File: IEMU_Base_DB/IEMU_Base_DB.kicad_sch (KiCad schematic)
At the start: 0 parts

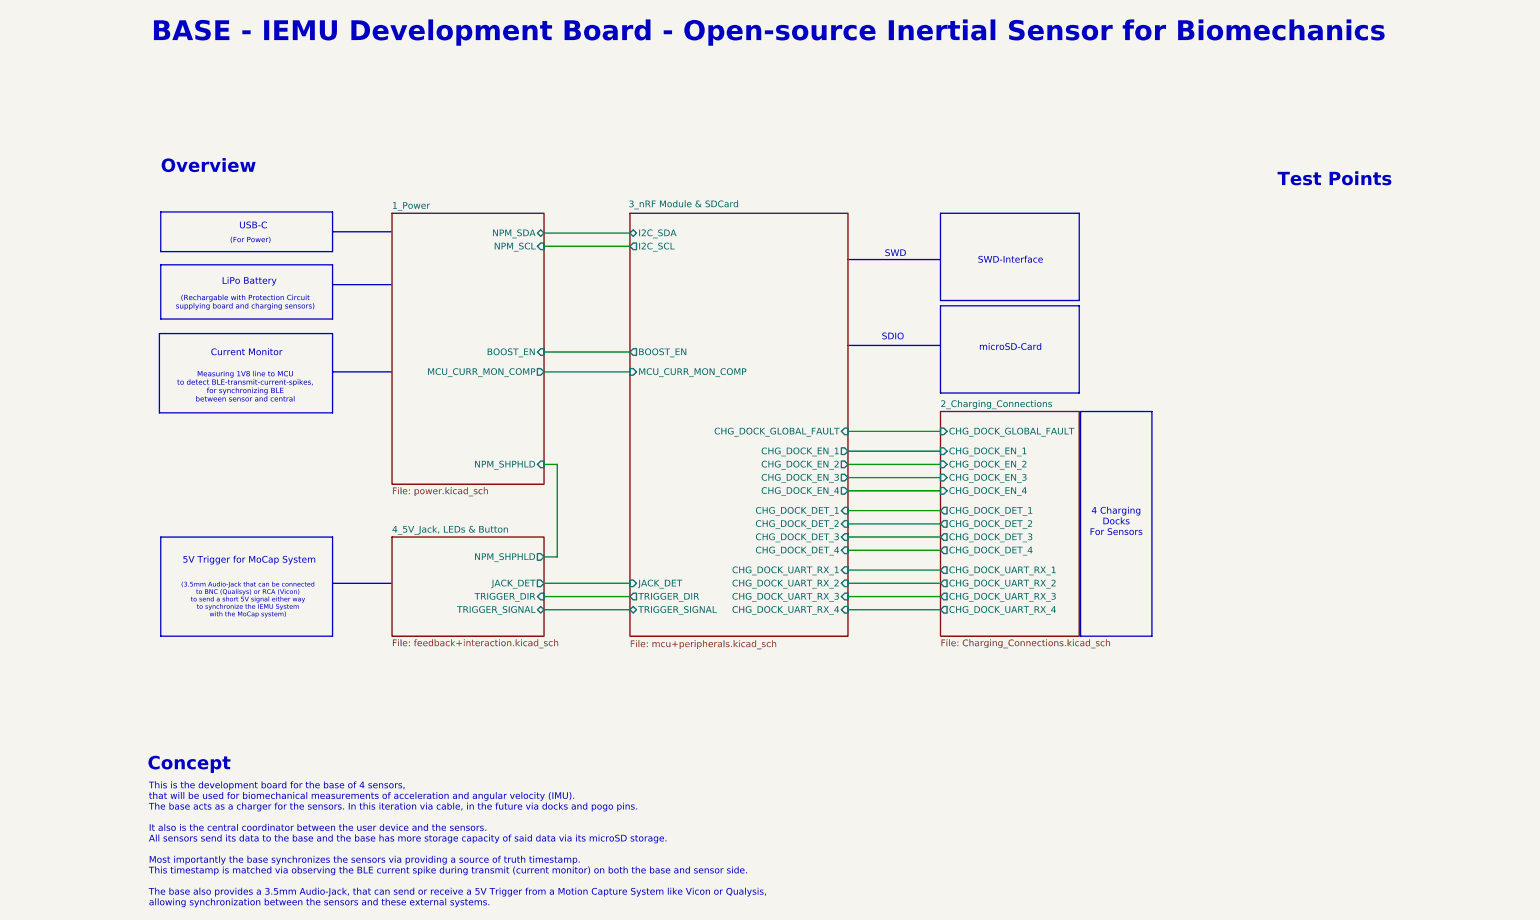
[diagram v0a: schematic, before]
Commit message: added hall effect sensor for lid detection
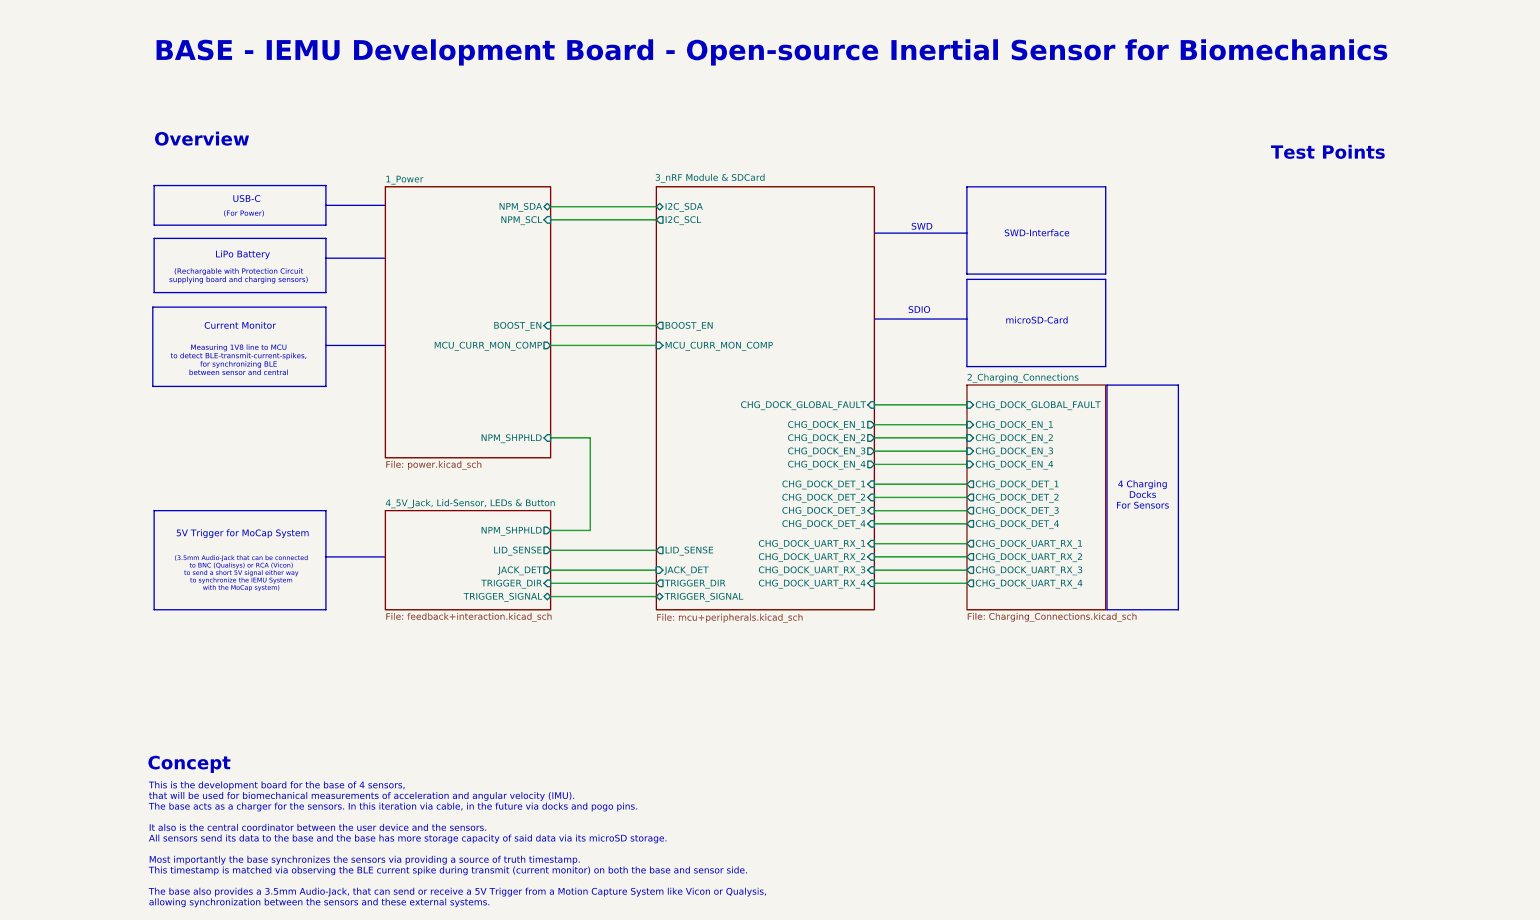
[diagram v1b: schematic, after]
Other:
- sheet 4_5V_Jack, LEDs & Button renamed 4_5V_Jack, Lid-Sensor, LEDs & Button
- sheet 3_nRF Module & SDCard ports: added LID_SENSE; removed none
- sheet 4_5V_Jack, Lid-Sensor, LEDs & Button ports: added LID_SENSE; removed none
